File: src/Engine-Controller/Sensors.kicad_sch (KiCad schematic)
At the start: 35 parts, among them P10 39299043, P11 39299043, P12 39299043, P13 39299043, P14 39299043, P15 39299043, P16 647676-2, P17 0530470410, P8 39299043, P9 39299043, U12 MAX4617EUE+T, U13 MAX4617EUE+T, U14 MCP96L01T-E_MX, U15 AD623ARZ-R7, U7 MC74HC4066ADG, U8 AD623ARZ-R7, U9 MC74HC4066ADG

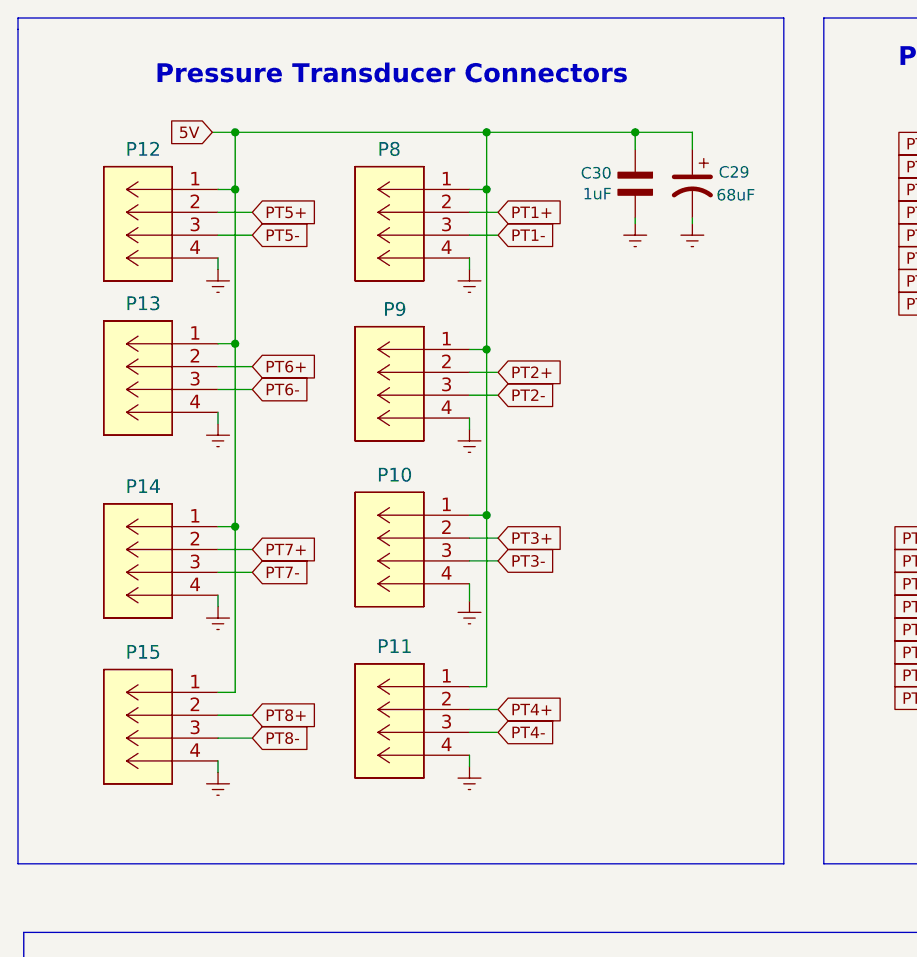
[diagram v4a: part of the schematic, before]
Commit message: changed pts to a single connector
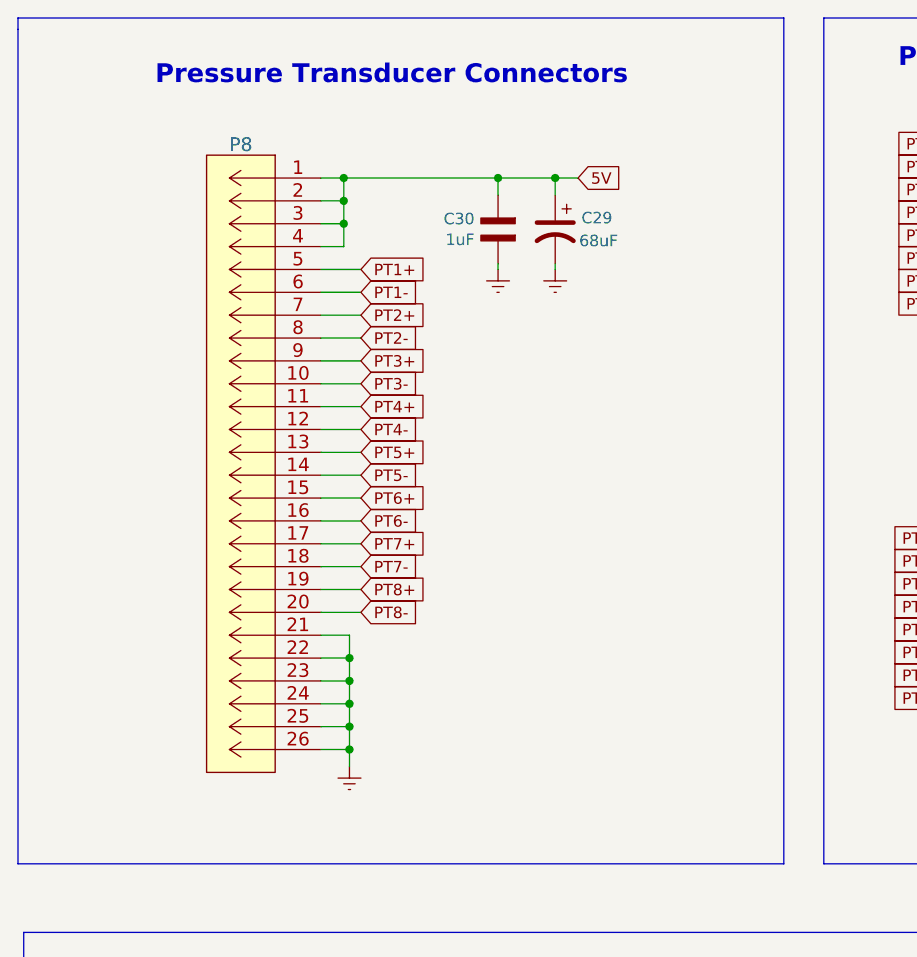
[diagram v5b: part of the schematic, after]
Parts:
- removed P10, P11, P12, P13, P14, P15, P8, P9: 39299043, CONN_4840.2201_SCH, symbol Engine-Controller:39299043
- added P8: 20021511-00026T4LF, CONN20_D10-RA-BK_SUL, symbol Engine-Controller:20021511-00026T4LF
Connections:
- net 5V: now also P8.1, P8.2, P8.3, P8.4
- net Earth: now also P8.21, P8.22, P8.23, P8.24, P8.25, P8.26
- net PT1+: now also P8.5
- net PT1-: now also P8.6
- net PT2+: now also P8.7
- net PT2-: now also P8.8
- net PT3+: now also P8.9
- net PT3-: now also P8.10
- net PT4+: now also P8.11
- net PT4-: now also P8.12
- net PT5+: now also P8.13
- net PT5-: now also P8.14
- net PT6+: now also P8.15
- net PT6-: now also P8.16
- net PT7+: now also P8.17
- net PT7-: now also P8.18
- net PT8+: now also P8.19
- net PT8-: now also P8.20
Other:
- moved on the sheet: C29, C30
